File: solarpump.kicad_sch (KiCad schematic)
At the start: 15 parts, among them J1 8-way_Screw, J13 SWD_IO, J2 UART_IO, J3 AUX_POWER, J4 USB_A, J5 Conn_DISP, J6 Conn_DISP

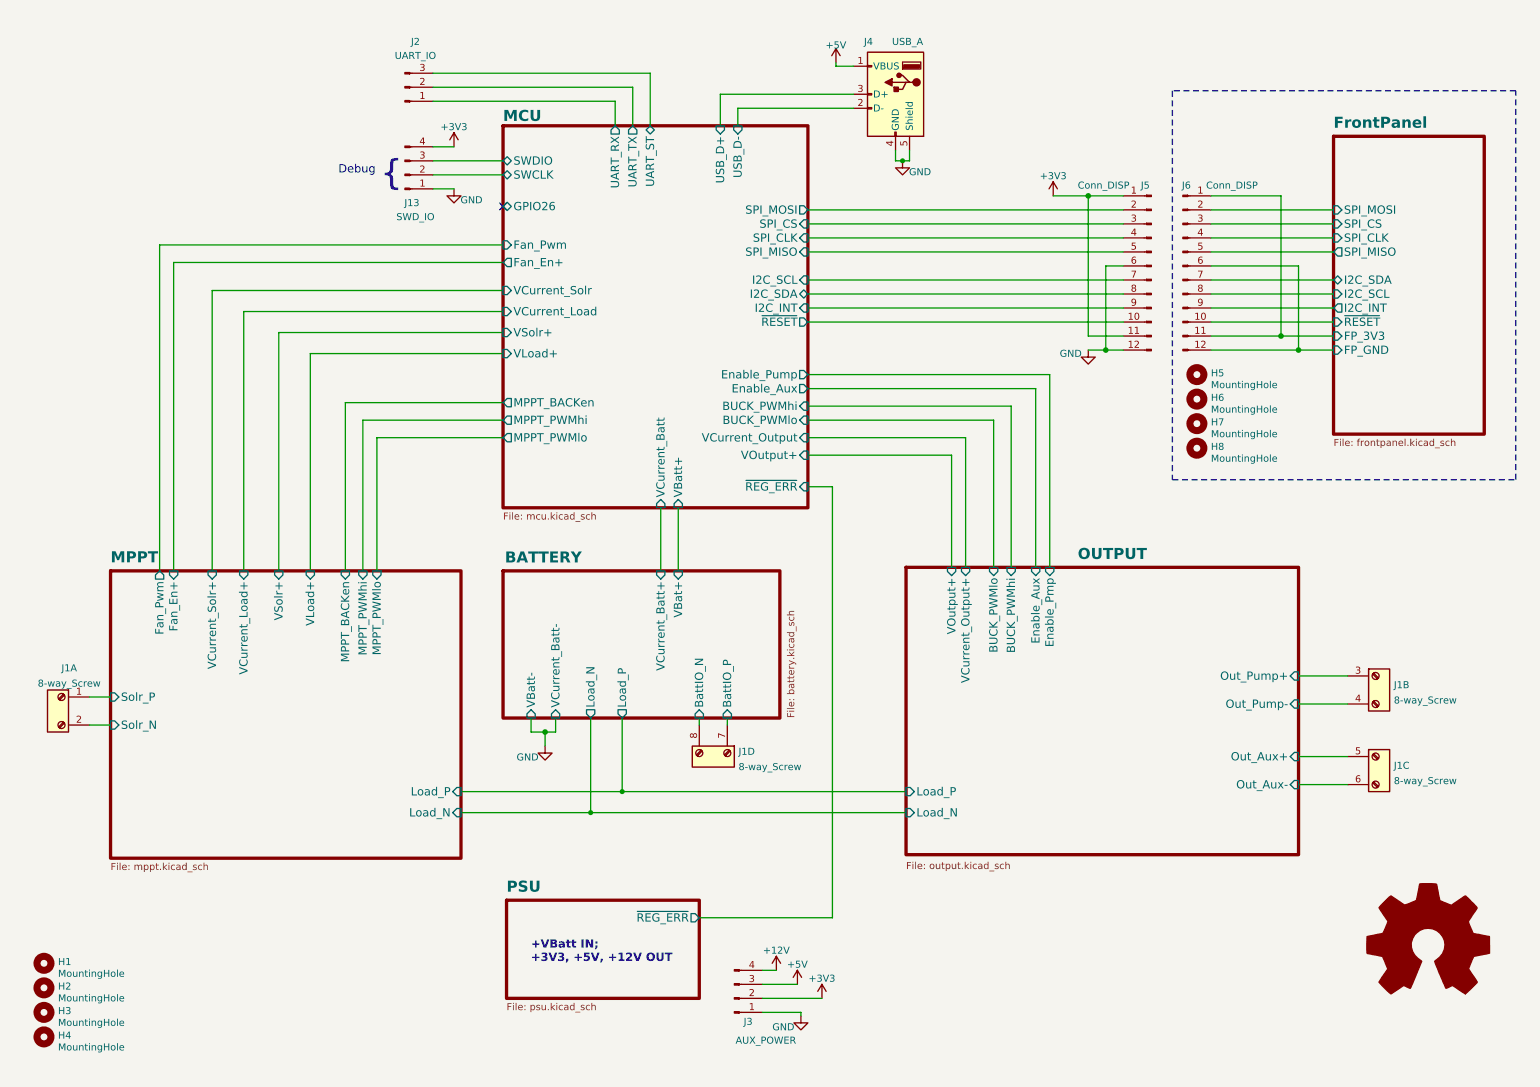
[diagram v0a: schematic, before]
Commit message: Adjust to supply 2 CS sigs to display; rename MISO to DC; larger conn cable.
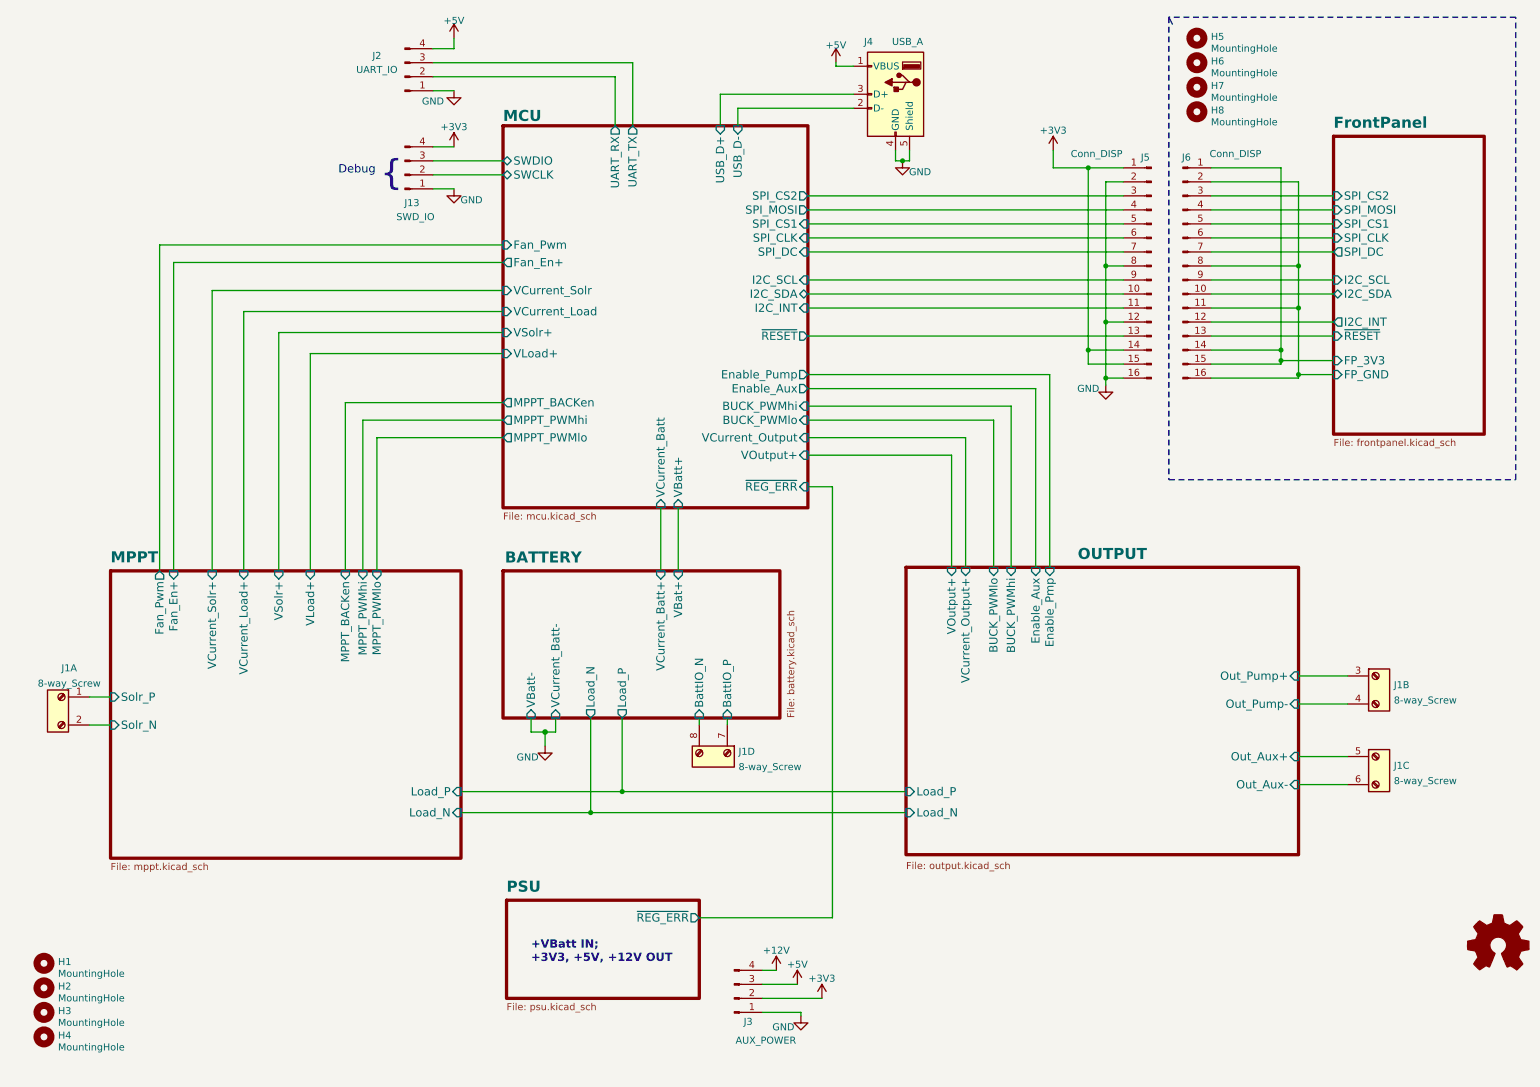
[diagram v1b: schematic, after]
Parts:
- J2: footprint Connector_PinHeader_2.00mm:PinHeader_1x03_P2.00mm_Vertical -> Connector_PinHeader_2.00mm:PinHeader_1x04_P2.00mm_Vertical; symbol Connector:Conn_01x03_Male -> Connector:Conn_01x04_Male
- J5, J6: footprint Connector_PinHeader_2.00mm:PinHeader_2x06_P2.00mm_Vertical -> Connector_PinHeader_2.00mm:PinHeader_2x08_P2.00mm_Vertical; symbol Connector:Conn_01x12_Male -> Connector:Conn_01x16_Male
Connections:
- net MCU/UART_ST is gone; now on net MCU/UART_TX: J2.3 (Pin_3)
- net +3V3: now also J5.14 (Pin_14), J5.15 (Pin_15); no longer J5.11 (Pin_11)
- net +5V: now also J2.4 (Pin_4)
- net FrontPanel/FP_3V3: now also J6.14 (Pin_14), J6.15 (Pin_15); no longer J6.11 (Pin_11)
- net FrontPanel/FP_GND: now also J6.11 (Pin_11), J6.16 (Pin_16), J6.2 (Pin_2), J6.8 (Pin_8); no longer J6.12 (Pin_12), J6.6 (Pin_6)
- net FrontPanel/I2C_INT: now also J6.12 (Pin_12); no longer J6.9 (Pin_9)
- net FrontPanel/I2C_SCL: now also J6.9 (Pin_9); no longer J6.8 (Pin_8)
- net FrontPanel/I2C_SDA: now also J6.10 (Pin_10); no longer J6.7 (Pin_7)
- net FrontPanel/SPI_CLK: now also J6.6 (Pin_6); no longer J6.4 (Pin_4)
- net FrontPanel/SPI_MOSI: now also J6.4 (Pin_4); no longer J6.2 (Pin_2)
- net FrontPanel/~{RESET}: now also J6.13 (Pin_13); no longer J6.10 (Pin_10)
- net GND: now also J2.1 (Pin_1), J5.16 (Pin_16), J5.2 (Pin_2), J5.8 (Pin_8); no longer J5.6 (Pin_6)
- net MCU/I2C_INT: now also J5.11 (Pin_11); no longer J5.9 (Pin_9)
- net MCU/I2C_SCL: now also J5.9 (Pin_9); no longer J5.7 (Pin_7)
- net MCU/I2C_SDA: now also J5.10 (Pin_10); no longer J5.8 (Pin_8)
- net MCU/SPI_CLK: now also J5.6 (Pin_6); no longer J5.4 (Pin_4)
- net MCU/SPI_MOSI: now also J5.4 (Pin_4); no longer J5.2 (Pin_2)
- net MCU/UART_RX: now also J2.2 (Pin_2); no longer J2.1 (Pin_1)
- net MCU/UART_TX: no longer J2.2 (Pin_2)
- net MCU/~{RESET}: now also J5.13 (Pin_13); no longer J5.10 (Pin_10)
- net FrontPanel/SPI_CS renamed FrontPanel/SPI_CS2
- net FrontPanel/SPI_MISO renamed FrontPanel/SPI_CS1
- net MCU/SPI_CS renamed MCU/SPI_CS2
- net MCU/SPI_MISO renamed MCU/SPI_CS1
- new net FrontPanel/SPI_DC: J6.7 (Pin_7)
- new net MCU/SPI_DC: J5.7 (Pin_7)
- no-connect marks 1 -> 0
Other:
- sheet FrontPanel ports: added SPI_CS1, SPI_CS2, SPI_DC; removed SPI_CS, SPI_MISO
- sheet MCU ports: added SPI_CS1, SPI_CS2, SPI_DC; removed GPIO26, SPI_CS, SPI_MISO, UART_ST
- moved on the sheet: H5, H6, H7, H8

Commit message: Lots of small changes; widen disp board to same as pwr board; use attiny mcu for rot-enc ctrl; switch to one board with cutline
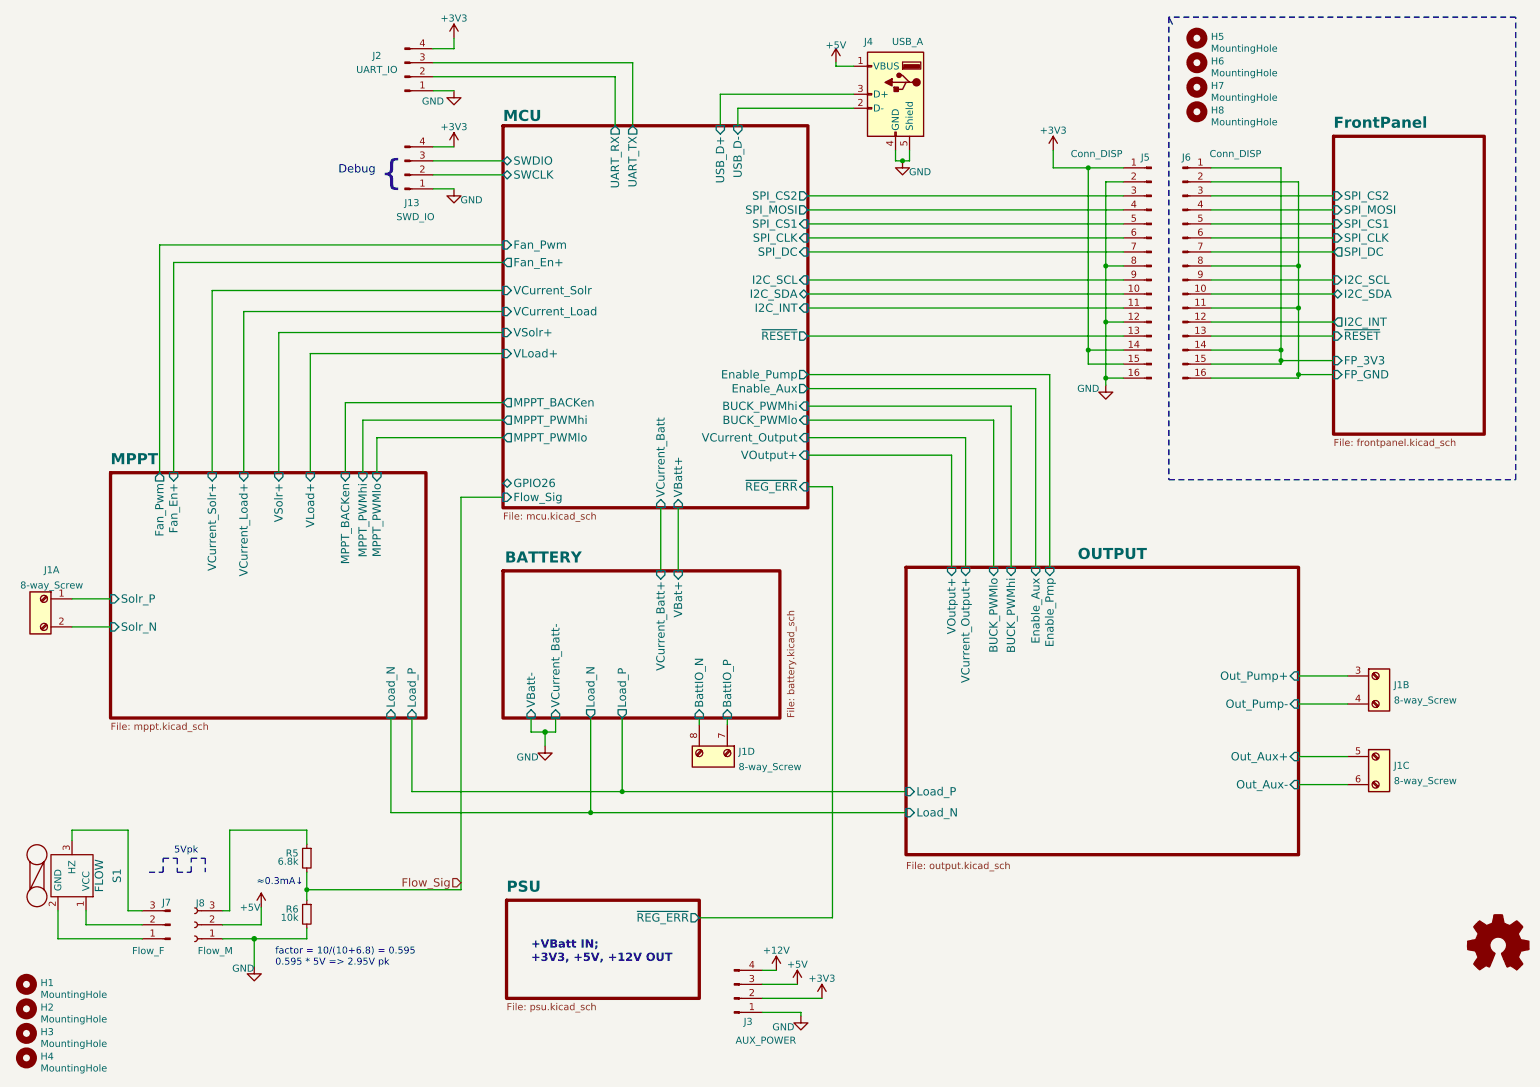
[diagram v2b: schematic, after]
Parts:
- added J7: Flow_F, symbol Connector:Conn_01x03_Male
- added J8: Flow_M, Connector:FanPinHeader_1x03_P2.54mm_Vertical, symbol Connector:Conn_01x03_Female
- added R5: 6.8k, Resistor_SMD:R_0805_2012Metric_Pad1.20x1.40mm_HandSolder, symbol Device:R_Small
- added R6: 10k, Resistor_SMD:R_0805_2012Metric_Pad1.20x1.40mm_HandSolder, symbol Device:R_Small
- added S1: FLOW, symbol solarpump:FLOW
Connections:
- net +3V3: now also J2.4 (Pin_4)
- net +5V: now also J8.2 (Pin_2); no longer J2.4 (Pin_4)
- net GND: now also J8.1 (Pin_1), R6.2
- new net: J8.3 (Pin_3), R5.1
- new net: J7.2 (Pin_2), S1.1 (VCC)
- new net: J7.1 (Pin_1), S1.2 (GND)
- new net: J7.3 (Pin_3), S1.3 (HZ)
- new net Flow_Sig: R5.2, R6.1
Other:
- sheet MCU ports: added Flow_Sig, GPIO26; removed none
- note added: "5Vpk"
- note added: "factor = 10/(10+6.8) = 0.595 0.595 * 5V => 2.95V pk"
- note added: "≈0.3mA↓"
- moved on the sheet: H1, H2, H3, H4, J1A

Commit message: Schematic + pcb 1.3.3
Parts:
- removed J13: SWD_IO, Connector_PinHeader_2.00mm:PinHeader_1x04_P2.00mm_Vertical, symbol Connector:Conn_01x04_Male
- added J13: JST SM03B-SRSS-TB, Connector_JST:JST_SH_SM03B-SRSS-TB_1x03-1MP_P1.00mm_Horizontal, symbol Connector_Generic_MountingPin:Conn_01x03_MountingPin
- added J17: USB_B_Micro, Connector_USB:USB_Micro-B_Molex_47346-0001, symbol Connector:USB_B_Micro
- added R53, R54: 10k, Resistor_SMD:R_0805_2012Metric_Pad1.20x1.40mm_HandSolder, symbol Device:R_Small
- added R55, R56: 100R, Resistor_SMD:R_0805_2012Metric_Pad1.20x1.40mm_HandSolder, symbol Device:R_Small
- H1, H2, H3, H4, H5, H6, H7, H8: value MountingHole -> Mount
- J4: now not fitted
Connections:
- net +3V3: now also R53.1, R54.1
- net +5V: now also J17.1 (VBUS)
- net FrontPanel/SPI_CS1: now also J6.3 (Pin_3); no longer J6.5 (Pin_5)
- net FrontPanel/SPI_CS2: now also J6.7 (Pin_7); no longer J6.3 (Pin_3)
- net FrontPanel/SPI_DC: now also J6.5 (Pin_5); no longer J6.7 (Pin_7)
- net GND: now also J13.2 (Pin_2), J13.MP (MountPin), J17.5 (GND), J17.6 (Shield)
- net MCU/SPI_CS1: now also J5.3 (Pin_3); no longer J5.5 (Pin_5)
- net MCU/SPI_CS2: now also J5.7 (Pin_7); no longer J5.3 (Pin_3)
- net MCU/SPI_DC: now also J5.5 (Pin_5); no longer J5.7 (Pin_7)
- net MCU/SWCLK: now also R53.2, R55.1
- net MCU/SWDIO: now also R54.2, R56.1
- net MCU/USB_D+: now also J17.3 (D+)
- net MCU/USB_D-: now also J17.2 (D-)
- net MCU/~{RESET} renamed ~{RESET}
- new net: J13.1 (Pin_1), R55.2
- new net: J13.3 (Pin_3), R56.2
- no-connect marks 0 -> 1
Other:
- note added: "SWD Debug"
- note removed: "Debug"
- note removed: "{"
